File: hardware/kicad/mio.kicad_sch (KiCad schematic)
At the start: 14 parts, among them SW901 RESET, SW902 PS_KEY, U201 xc7z007sclg225, U901 33.3333MHz

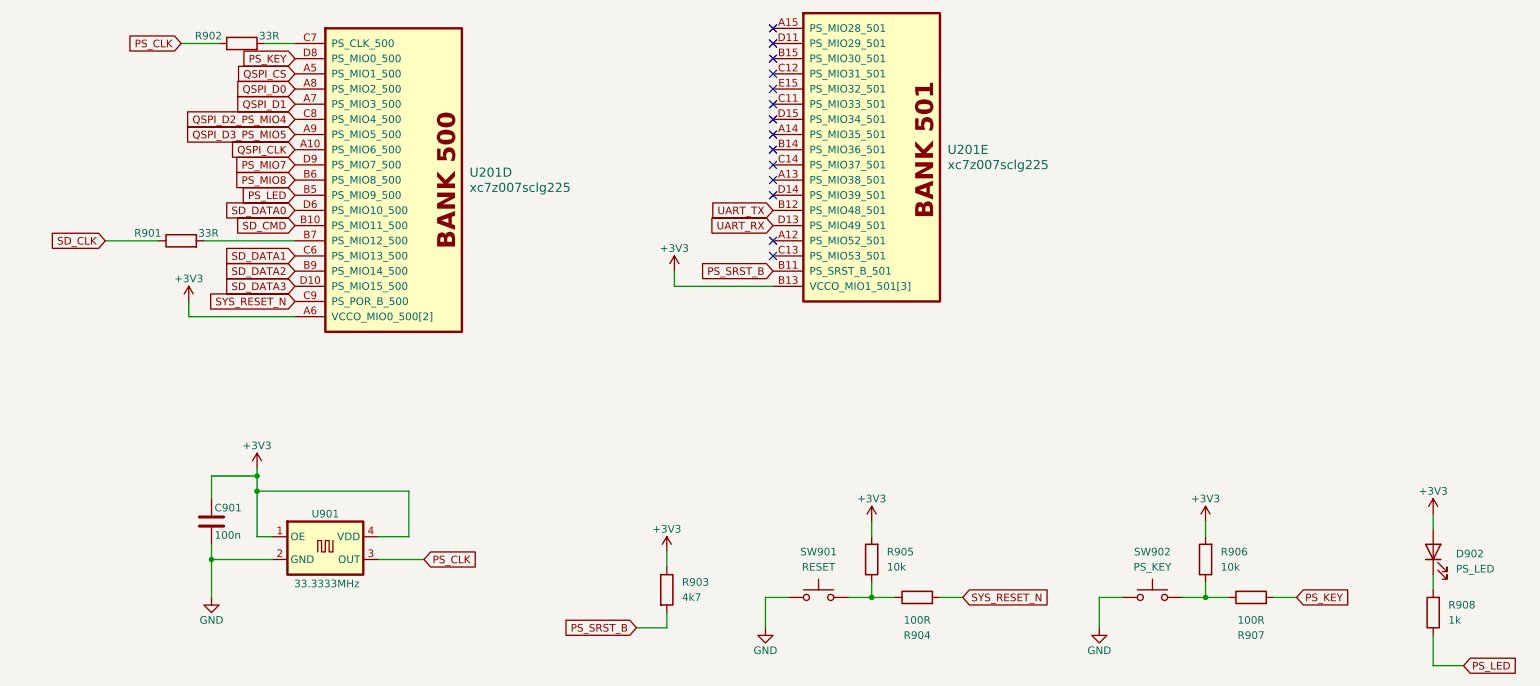
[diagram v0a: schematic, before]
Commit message: finish basic ddr routing
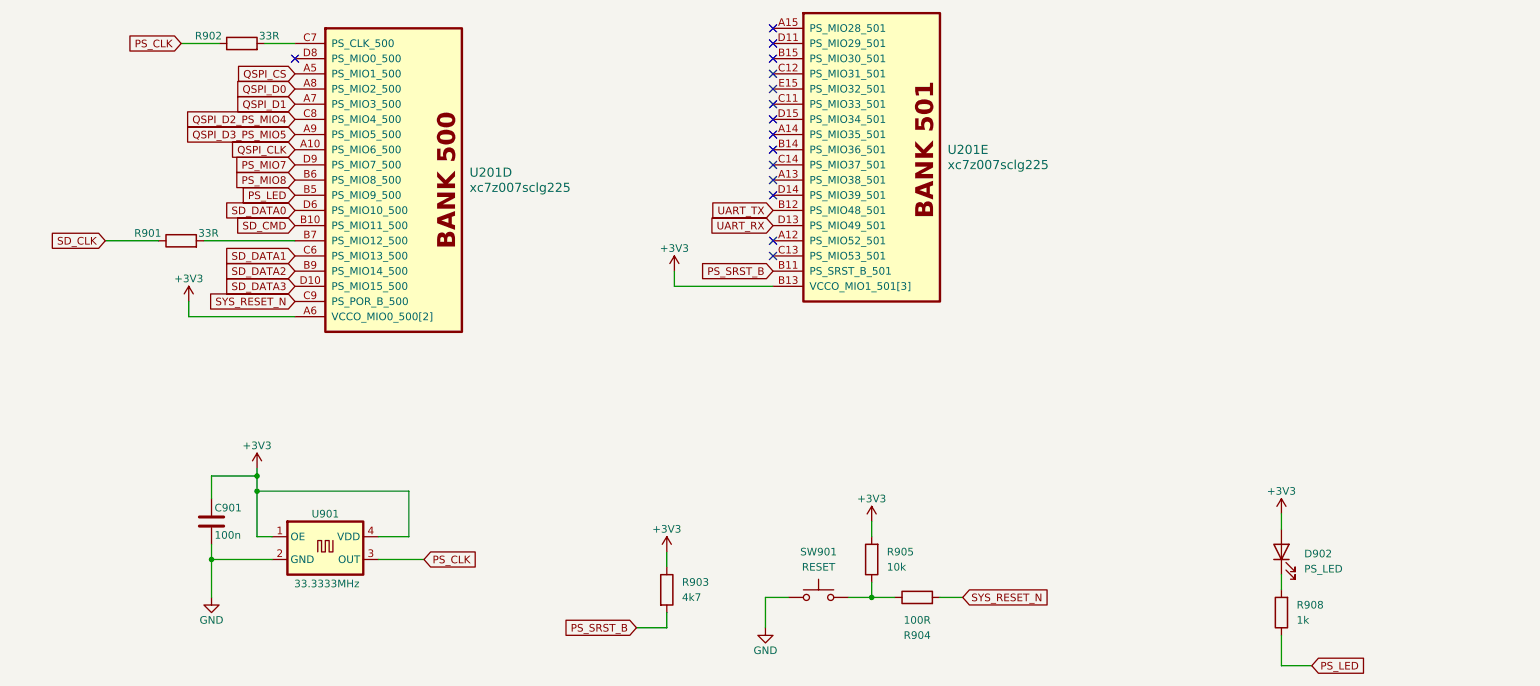
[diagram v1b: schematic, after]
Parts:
- removed R906: 10k, Resistor_SMD:R_0402_1005Metric, symbol Device:R
- removed R907: 100R, Resistor_SMD:R_0402_1005Metric, symbol Device:R
- removed SW902: PS_KEY, Button_Switch_SMD:SW_Tactile_SPST_NO_Straight_CK_PTS636Sx25SMTRLFS, symbol Switch:SW_Push
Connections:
- net PS_KEY: no longer names the net of U201.D8 (PS_MIO0_500)
- no-connect marks 14 -> 15
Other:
- moved on the sheet: D902, R908

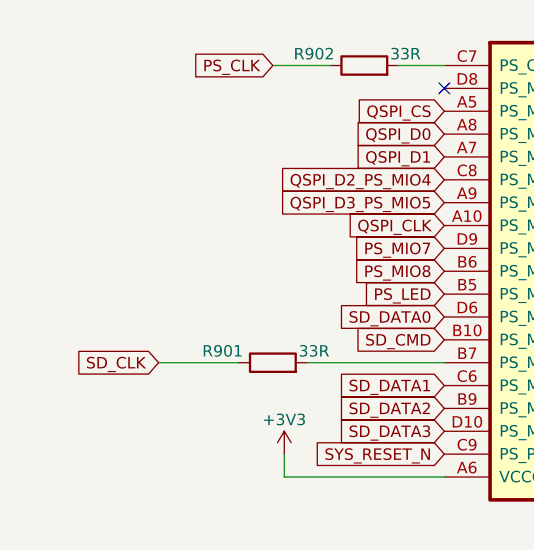
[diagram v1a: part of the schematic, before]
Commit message: feat: need switch two singals of SD inferface
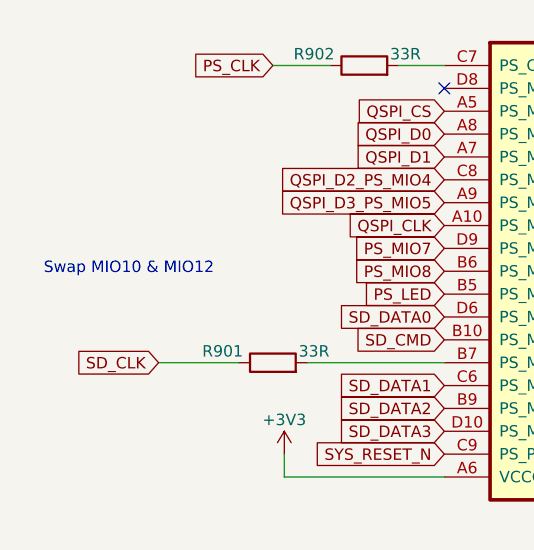
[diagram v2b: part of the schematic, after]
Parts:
- R901, R902, R904, R905: footprint Resistor_SMD:R_0402_1005Metric -> Resistor_SMD:R_0603_1608Metric
- U201: footprint Package_BGA:Xilinx_CLG225 -> (none)
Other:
- note added: "Swap MIO10 & MIO12"
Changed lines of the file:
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@@
 	(generator_version "10.0")
 	(paper "A4")
+	(text "Swap MIO10 & MIO12\n"
+		(exclude_from_sim no)
+		(at 33.528 58.166 0)
+		(effects
+			(font
+				(size 1.27 1.27)
+			)
+		)
+	)
 	(junction
 		(at 62.23 107.95)
@@
 			)
 		)
-		(property "Footprint" "Resistor_SMD:R_0402_1005Metric"
+		(property "Footprint" "Resistor_SMD:R_0603_1608Metric"
 			(at 172.72 130.048 90)
 			(hide yes)
@@
 			)
 		)
-		(property "Footprint" "Resistor_SMD:R_0402_1005Metric"
+		(property "Footprint" "Resistor_SMD:R_0603_1608Metric"
 			(at 166.878 121.92 90)
 			(hide yes)
@@
 	)
 	(symbol
+		(lib_name "xc7z007sclg225_1")
 		(lib_id "Xilinx7:xc7z007sclg225")
 		(at 68.58 35.56 0)
@@
 			)
 		)
-		(property "Footprint" "Package_BGA:Xilinx_CLG225"
+		(property "Footprint" ""
 			(at 73.66 34.29 0)
 			(hide yes)
@@
 			)
 		)
-		(property "Footprint" "Resistor_SMD:R_0402_1005Metric"
+		(property "Footprint" "Resistor_SMD:R_0603_1608Metric"
 			(at 49.53 70.358 90)
 			(hide yes)
@@
 			)
 		)
-		(property "Footprint" "Resistor_SMD:R_0402_1005Metric"
+		(property "Footprint" "Resistor_SMD:R_0603_1608Metric"
 			(at 59.69 37.338 90)
 			(hide yes)
@@
 			)
 		)
-		(property "Footprint" "Package_BGA:Xilinx_CLG225"
+		(property "Footprint" ""
 			(at 153.67 31.75 0)
 			(hide yes)
